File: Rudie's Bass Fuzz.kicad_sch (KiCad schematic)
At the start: 13 parts, among them J1 Conn_01x01_Male, J2 Conn_01x01_Male, J3 Conn_01x01_Male, J4 Conn_01x01_Male, Q1 BC549

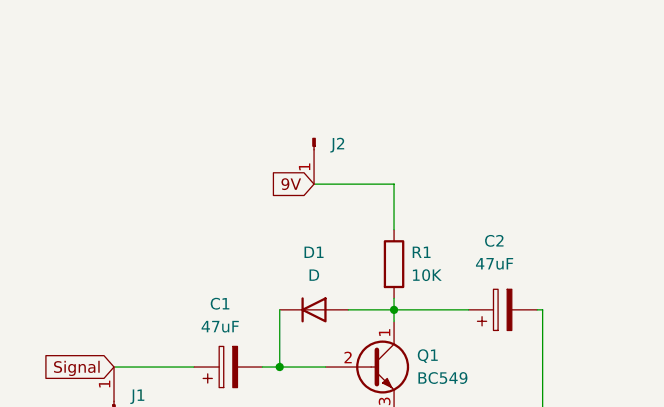
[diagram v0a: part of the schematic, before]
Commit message: added power LED
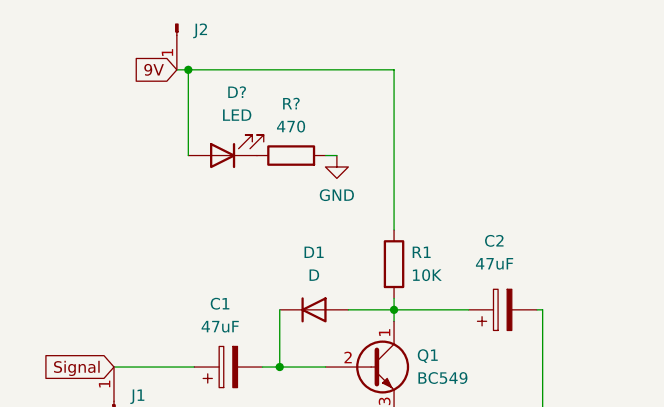
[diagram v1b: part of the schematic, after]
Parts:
- added D?: LED, symbol Device:LED
- added R?: 470, Resistor_THT:R_Axial_DIN0207_L6.3mm_D2.5mm_P10.16mm_Horizontal, symbol Device:R
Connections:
- net 9V: now also D?.2 (A)
- net GND: now also R?.2
- new net: D?.1 (K), R?.1
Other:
- moved on the sheet: J2
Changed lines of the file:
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@@
   (junction (at 94.615 71.12) (diameter 0) (color 0 0 0 0)
   )
+  (junction (at 84.455 38.1) (diameter 0) (color 0 0 0 0)
+  )
   (wire (pts (xy 94.615 64.77) (xy 94.615 71.12))
     (stroke (width 0) (type default) (color 0 0 0 0))
   )
+  (wire (pts (xy 107.315 38.1) (xy 107.315 55.88))
+    (stroke (width 0) (type default) (color 0 0 0 0))
+  )
+  (wire (pts (xy 84.455 38.1) (xy 107.315 38.1))
+    (stroke (width 0) (type default) (color 0 0 0 0))
+  )
   (wire (pts (xy 76.2 71.12) (xy 85.09 71.12))
     (stroke (width 0) (type default) (color 0 0 0 0))
@@
     (stroke (width 0) (type default) (color 0 0 0 0))
   )
-  (wire (pts (xy 107.315 50.8) (xy 107.315 55.88))
+  (wire (pts (xy 99.695 47.625) (xy 100.965 47.625))
     (stroke (width 0) (type default) (color 0 0 0 0))
   )
@@
     (stroke (width 0) (type default) (color 0 0 0 0))
   )
+  (wire (pts (xy 84.455 38.1) (xy 84.455 47.625))
+    (stroke (width 0) (type default) (color 0 0 0 0))
+  )
   (wire (pts (xy 107.315 63.5) (xy 107.315 64.77))
     (stroke (width 0) (type default) (color 0 0 0 0))
   )
-  (wire (pts (xy 98.425 50.8) (xy 107.315 50.8))
+  (wire (pts (xy 83.185 38.1) (xy 84.455 38.1))
     (stroke (width 0) (type default) (color 0 0 0 0))
   )
@@
     )
   )
-  (global_label "9V" (shape input) (at 98.425 50.8 180) (fields_autoplaced)
+  (global_label "9V" (shape input) (at 83.185 38.1 180) (fields_autoplaced)
     (effects (font (size 1.27 1.27)) (justify right))
-    (property "Intersheet References" "${INTERSHEET_REFS}" (id 0) (at 93.7138 50.7206 0)
+    (property "Intersheet References" "${INTERSHEET_REFS}" (id 0) (at 78.4738 38.0206 0)
       (effects (font (size 1.27 1.27)) (justify right) hide)
     )
@@
     (pin "3")
   )
+  (symbol (lib_id "power:GND") (at 100.965 47.625 0) (unit 1)
+    (in_bom yes) (on_board yes) (fields_autoplaced)
+    (property "Reference" "#PWR?" (id 0) (at 100.965 53.975 0)
+      (effects (font (size 1.27 1.27)) hide)
+    )
+    (property "Value" "GND" (id 1) (at 100.965 52.07 0))
+    (property "Footprint" "" (id 2) (at 100.965 47.625 0)
+      (effects (font (size 1.27 1.27)) hide)
+    )
+    (property "Datasheet" "" (id 3) (at 100.965 47.625 0)
+      (effects (font (size 1.27 1.27)) hide)
+    )
+    (pin "1")
+  )
   (symbol (lib_id "Connector:Conn_01x01_Male") (at 141.605 74.93 270) (unit 1)
     (in_bom yes) (on_board yes) (fields_autoplaced)
@@
     )
     (pin "1")
+  )
+  (symbol (lib_id "Device:R") (at 95.885 47.625 90) (unit 1)
+    (in_bom yes) (on_board yes) (fields_autoplaced)
+    (property "Reference" "R?" (id 0) (at 95.885 41.91 90))
+    (property "Value" "470" (id 1) (at 95.885 44.45 90))
+    (property "Footprint" "Resistor_THT:R_Axial_DIN0207_L6.3mm_D2.5mm_P10.16mm_Horizontal" (id 2) (at 95.885 49.403 90)
+      (effects (font (size 1.27 1.27)) hide)
+    )
+    (property "Datasheet" "~" (id 3) (at 95.885 47.625 0)
+      (effects (font (size 1.27 1.27)) hide)
+    )
+    (pin "1")
+    (pin "2")
   )
   (symbol (lib_id "Device:C_Polarized") (at 88.9 71.12 90) (unit 1)
@@
     )
   )
+  (symbol (lib_id "Device:LED") (at 88.265 47.625 180) (unit 1)
+    (in_bom yes) (on_board yes) (fields_autoplaced)
+    (property "Reference" "D?" (id 0) (at 89.8525 40.64 0))
+    (property "Value" "LED" (id 1) (at 89.8525 43.18 0))
+    (property "Footprint" "" (id 2) (at 88.265 47.625 0)
+      (effects (font (size 1.27 1.27)) hide)
+    )
+    (property "Datasheet" "~" (id 3) (at 88.265 47.625 0)
+      (effects (font (size 1.27 1.27)) hide)
+    )
+    (pin "1")
+    (pin "2")
+  )
   (symbol (lib_id "Device:D") (at 98.425 64.77 0) (unit 1)
     (in_bom yes) (on_board yes) (fields_autoplaced)
@@
     (pin "2")
   )
-  (symbol (lib_id "Connector:Conn_01x01_Male") (at 98.425 45.72 270) (unit 1)
-    (in_bom yes) (on_board yes) (fields_autoplaced)
-    (property "Reference" "J2" (id 0) (at 100.33 46.3549 90)
-      (effects (font (size 1.27 1.27)) (justify left))
-    )
-    (property "Value" "Conn_01x01_Male" (id 1) (at 99.695 47.6249 90)
+  (symbol (lib_id "Connector:Conn_01x01_Male") (at 83.185 33.02 270) (unit 1)
+    (in_bom yes) (on_board yes) (fields_autoplaced)
+    (property "Reference" "J2" (id 0) (at 85.09 33.6549 90)
+      (effects (font (size 1.27 1.27)) (justify left))
+    )
+    (property "Value" "Conn_01x01_Male" (id 1) (at 84.455 34.9249 90)
       (effects (font (size 1.27 1.27)) (justify left) hide)
     )
-    (property "Footprint" "Connector_Pin:Pin_D1.4mm_L8.5mm_W2.8mm_FlatFork" (id 2) (at 98.425 45.72 0)
-      (effects (font (size 1.27 1.27)) hide)
-    )
-    (property "Datasheet" "~" (id 3) (at 98.425 45.72 0)
+    (property "Footprint" "Connector_Pin:Pin_D1.4mm_L8.5mm_W2.8mm_FlatFork" (id 2) (at 83.185 33.02 0)
+      (effects (font (size 1.27 1.27)) hide)
+    )
+    (property "Datasheet" "~" (id 3) (at 83.185 33.02 0)
       (effects (font (size 1.27 1.27)) hide)
     )
@@
       (reference "#PWR02") (unit 1) (value "GND") (footprint "")
     )
+    (path "/62bdca84-5f08-4fac-a6cd-57f74c0bfc94"
+      (reference "#PWR?") (unit 1) (value "GND") (footprint "")
+    )
     (path "/8654b05d-362b-4cb4-926f-93b0a01dc527"
       (reference "C1") (unit 1) (value "47uF") (footprint "Capacitor_THT:CP_Radial_D5.0mm_P2.50mm")
@@
       (reference "D1") (unit 1) (value "D") (footprint "Diode_THT:D_A-405_P12.70mm_Horizontal")
     )
+    (path "/9bac20ab-0eff-4b4e-96fd-8a8eb787d966"
+      (reference "D?") (unit 1) (value "LED") (footprint "")
+    )
     (path "/0309e1ab-0658-4dbf-89ab-e051ee8674ac"
       (reference "H1") (unit 1) (value "MountingHole") (footprint "MountingHole:MountingHole_3.2mm_M3")
@@
       (reference "R1") (unit 1) (value "10K") (footprint "Resistor_THT:R_Axial_DIN0207_L6.3mm_D2.5mm_P10.16mm_Horizontal")
     )
+    (path "/81632b8d-e4b9-482a-84dd-cfc8f01f89ad"
+      (reference "R?") (unit 1) (value "470") (footprint "Resistor_THT:R_Axial_DIN0207_L6.3mm_D2.5mm_P10.16mm_Horizontal")
+    )
     (path "/57d2b19e-4c2f-4903-ba5c-1c3fdf03f50d"

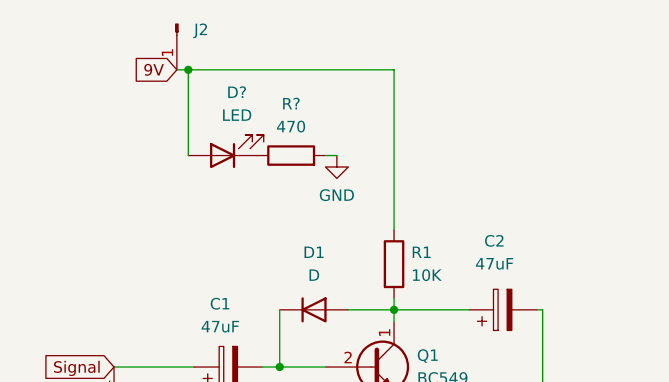
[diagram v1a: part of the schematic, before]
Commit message: annotated led components
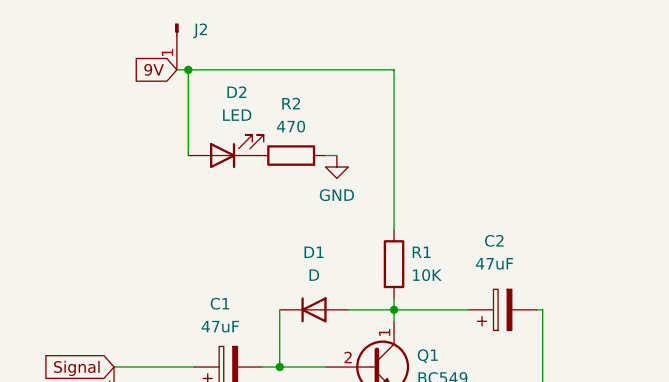
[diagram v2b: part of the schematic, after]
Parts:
- gave numbers to parts that had none: 2
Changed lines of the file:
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@@
   (symbol (lib_id "power:GND") (at 100.965 47.625 0) (unit 1)
     (in_bom yes) (on_board yes) (fields_autoplaced)
-    (property "Reference" "#PWR?" (id 0) (at 100.965 53.975 0)
+    (property "Reference" "#PWR03" (id 0) (at 100.965 53.975 0)
       (effects (font (size 1.27 1.27)) hide)
     )
@@
   (symbol (lib_id "Device:R") (at 95.885 47.625 90) (unit 1)
     (in_bom yes) (on_board yes) (fields_autoplaced)
-    (property "Reference" "R?" (id 0) (at 95.885 41.91 90))
+    (property "Reference" "R2" (id 0) (at 95.885 41.91 90))
     (property "Value" "470" (id 1) (at 95.885 44.45 90))
     (property "Footprint" "Resistor_THT:R_Axial_DIN0207_L6.3mm_D2.5mm_P10.16mm_Horizontal" (id 2) (at 95.885 49.403 90)
@@
   (symbol (lib_id "Device:LED") (at 88.265 47.625 180) (unit 1)
     (in_bom yes) (on_board yes) (fields_autoplaced)
-    (property "Reference" "D?" (id 0) (at 89.8525 40.64 0))
+    (property "Reference" "D2" (id 0) (at 89.8525 40.64 0))
     (property "Value" "LED" (id 1) (at 89.8525 43.18 0))
     (property "Footprint" "" (id 2) (at 88.265 47.625 0)
@@
     )
     (path "/62bdca84-5f08-4fac-a6cd-57f74c0bfc94"
-      (reference "#PWR?") (unit 1) (value "GND") (footprint "")
+      (reference "#PWR03") (unit 1) (value "GND") (footprint "")
     )
     (path "/8654b05d-362b-4cb4-926f-93b0a01dc527"
@@
     )
     (path "/9bac20ab-0eff-4b4e-96fd-8a8eb787d966"
-      (reference "D?") (unit 1) (value "LED") (footprint "")
+      (reference "D2") (unit 1) (value "LED") (footprint "")
     )
     (path "/0309e1ab-0658-4dbf-89ab-e051ee8674ac"
@@
     )
     (path "/81632b8d-e4b9-482a-84dd-cfc8f01f89ad"
-      (reference "R?") (unit 1) (value "470") (footprint "Resistor_THT:R_Axial_DIN0207_L6.3mm_D2.5mm_P10.16mm_Horizontal")
+      (reference "R2") (unit 1) (value "470") (footprint "Resistor_THT:R_Axial_DIN0207_L6.3mm_D2.5mm_P10.16mm_Horizontal")
     )
     (path "/57d2b19e-4c2f-4903-ba5c-1c3fdf03f50d"
